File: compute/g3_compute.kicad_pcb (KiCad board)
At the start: 4 copper layers, 100 x 100 mm, 67 parts, among them J101 CONSMA001-SMD-G, J102 Temp_Connector_1x4, J103 Conn_02x03_Counter_Clockwise, J104 Conn_Power_Compute_02x05, J3 GPIO_Breakout_Conn, U101 PA1616D, U102 LoRa-E5, U201 SX1262, U202 PE4259, Y201 TBD

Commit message: changes to compute
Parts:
- moved U101 28.2 mm to (81.7, 47.2)
- moved J103 20.5 mm to (132.2, 155.2)
- moved J104 20.5 mm to (120.0, 155.2)
- moved J3 20.5 mm to (105.5, 155.1)
- moved J102 20.3 mm to (156.6, 21.8)

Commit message: fixes to power and compute
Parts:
- removed the C102 at (186.2, 69.0)
- removed the C102 at (192.2, 20.5)
- removed C201: 470nF, Capacitor_SMD:C_0402_1005Metric_Pad0.74x0.62mm_HandSolder
- removed C202: 100nF, Capacitor_SMD:C_0402_1005Metric_Pad0.74x0.62mm_HandSolder
- removed C203: 1uF, Capacitor_SMD:C_0402_1005Metric_Pad0.74x0.62mm_HandSolder
- removed C204: 47nF, Capacitor_SMD:C_0402_1005Metric_Pad0.74x0.62mm_HandSolder
- removed C205: 47pF, Capacitor_SMD:C_0402_1005Metric_Pad0.74x0.62mm_HandSolder
- removed C206, C213: 1.8pF, Capacitor_SMD:C_0402_1005Metric_Pad0.74x0.62mm_HandSolder
- removed C207, C210: 4.7pF, Capacitor_SMD:C_0402_1005Metric_Pad0.74x0.62mm_HandSolder
- removed C208: 2.4pF, Capacitor_SMD:C_0402_1005Metric_Pad0.74x0.62mm_HandSolder
- removed C209: 3pF, Capacitor_SMD:C_0402_1005Metric_Pad0.74x0.62mm_HandSolder
- removed C211: 5.6pF, Capacitor_SMD:C_0402_1005Metric_Pad0.74x0.62mm_HandSolder
- removed C212, C215: 39pF, Capacitor_SMD:C_0402_1005Metric_Pad0.74x0.62mm_HandSolder
- removed C214: 1nF, Capacitor_SMD:C_0402_1005Metric_Pad0.74x0.62mm_HandSolder
- removed C216, C217: 3.3pF, Capacitor_SMD:C_0402_1005Metric_Pad0.74x0.62mm_HandSolder
- removed J103: Conn_02x03_Counter_Clockwise, Connector_Samtec_HLE_SMD:Samtec_HLE-103-02-xxx-DV_2x03_P2.54mm_Horizontal
- removed J104: Conn_Power_Compute_02x05, Connector_Samtec_HLE_SMD:Samtec_HLE-105-02-xxx-DV_2x05_P2.54mm_Horizontal
- removed J3: GPIO_Breakout_Conn, Connector_Samtec_HLE_SMD:Samtec_HLE-105-02-xxx-DV_2x05_P2.54mm_Horizontal
- removed L201: 15uH, Inductor_SMD:L_0805_2012Metric_Pad1.05x1.20mm_HandSolder
- removed L202: 0H, Inductor_SMD:L_0402_1005Metric_Pad0.77x0.64mm_HandSolder
- removed L203: 15nH, Inductor_SMD:L_0402_1005Metric_Pad0.77x0.64mm_HandSolder
- removed L204: 47nH, Inductor_SMD:L_0402_1005Metric_Pad0.77x0.64mm_HandSolder
- removed L205: 2.5nH, Inductor_SMD:L_0402_1005Metric_Pad0.77x0.64mm_HandSolder
- removed L206: 4.7nH, Inductor_SMD:L_0402_1005Metric_Pad0.77x0.64mm_HandSolder
- removed L207: 9.1nH, Inductor_SMD:L_0402_1005Metric_Pad0.77x0.64mm_HandSolder
- removed R201: 100, Resistor_SMD:R_0402_1005Metric_Pad0.72x0.64mm_HandSolder
- removed TP110: TestPoint, Capacitor_SMD:C_0805_2012Metric_Pad1.18x1.45mm_HandSolder
- removed U201: SX1262, Package_DFN_QFN:QFN-24-1EP_4x4mm_P0.5mm_EP2.7x2.7mm
- removed U202: PE4259, Package_TO_SOT_SMD:SOT-363_SC-70-6
- removed Y201: TBD, Crystal:Crystal_SMD_2016-4Pin_2.0x1.6mm
- added C102: 4.7uF, Capacitor_SMD:C_0402_1005Metric_Pad0.74x0.62mm_HandSolder, F.Cu at (151.4, 51.7)
- added J1: Conn_01x10_Female, Connector_Molex:Molex_CLIK-Mate_502386-1070_1x10-1MP_P1.25mm_Horizontal, F.Cu at (138.7, 98.5)
- added J2: Conn_01x10_Female, Connector_Molex:Molex_CLIK-Mate_502386-1070_1x10-1MP_P1.25mm_Horizontal, F.Cu at (138.8, 119.9)
- added TP1: TestPoint, Capacitor_SMD:C_0805_2012Metric_Pad1.18x1.45mm_HandSolder, F.Cu at (160.5, 148.1)
- added TP2: TestPoint, Capacitor_SMD:C_0805_2012Metric_Pad1.18x1.45mm_HandSolder, F.Cu at (150.9, 148.1)
- added TP3: TestPoint, Capacitor_SMD:C_0805_2012Metric_Pad1.18x1.45mm_HandSolder, F.Cu at (155.7, 145.1)
- moved U101 115.6 mm to (190.7, 85.9), turned to 90 degrees
- moved J101 98.0 mm to (192.3, 143.7), turned to 270 degrees
- moved J102 94.8 mm to (187.1, 111.6), turned to 90 degrees
- moved R301 94.5 mm to (161.5, 47.7)
- moved C104 93.4 mm to (186.6, 143.9), turned to 270 degrees
- moved C103 89.3 mm to (184.7, 140.6), turned to 270 degrees
- moved L101 88.3 mm to (186.6, 140.6), turned to 270 degrees
- moved TP115 87.6 mm to (170.1, 148.1), turned to 0 degrees
- moved TP103 84.7 mm to (160.5, 145.1), turned to 0 degrees
- moved TP106 82.6 mm to (165.3, 145.1), turned to 0 degrees
- moved TP112 82.6 mm to (170.1, 145.1), turned to 0 degrees
- moved TP114 82.4 mm to (165.3, 151.1), turned to 0 degrees
- moved TP105 80.5 mm to (155.7, 151.1), turned to 0 degrees
- moved TP111 79.8 mm to (165.3, 148.1), turned to 0 degrees
- moved R101 79.5 mm to (144.9, 47.7)
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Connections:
- net /GPS_VCC renamed /GPS_Switch/VOUT
- net 3V3 renamed +3V3
- net 5V renamed +5V
- A101 pad 11: /PI_GPIO17 -> /PS_VSolSense
- A101 pad 12: /PI_GPIO18 -> /~PS_CC_QON
- A101 pad 16: /PI_GPIO23 -> /~PS_CC_INT
- A101 pad 18: /PI_GPIO24 -> /~PC_CC_CE
- A101 pad 22: /PI_GPIO25 -> /PS_VR_PS
- A101 pad 32: /PI_INT -> /CPPC_INT
- A101 pad 7: /PI_GPIO4 -> /PS_VBatSense
- J102 pad 4: /PI_SDL -> /PI_SCL
- R104 pad 1: /PI_SDL -> /PI_SCL
- TP109 pad 1: /PI_SDL -> /PI_SCL
- U102 pad 16: Net-(U102-Pad16) -> GND
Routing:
- net GND: track 53.4 -> 0.00 mm, vias 15 -> 0
- net /ANT: track 21.9 -> 0.00 mm
- net Net-(C204-Pad1): track 7.09 -> 0.00 mm
- net +3V3: track 6.70 -> 0.00 mm, vias 3 -> 0
- net Net-(U201-Pad4): track 6.52 -> 0.00 mm
- net Net-(C214-Pad1): track 6.44 -> 0.00 mm
- net Net-(C207-Pad1): track 5.38 -> 0.00 mm
- net Net-(C201-Pad1): track 5.19 -> 0.00 mm
- net Net-(L202-Pad1): track 5.07 -> 0.00 mm
- net Net-(C206-Pad1): track 4.97 -> 0.00 mm
- net Net-(L203-Pad1): track 4.14 -> 0.00 mm
- net Net-(C209-Pad2): track 3.58 -> 0.00 mm
- net Net-(U201-Pad3): track 3.58 -> 0.00 mm
- net Net-(L201-Pad2): track 2.79 -> 0.00 mm
- net Net-(C213-Pad1): track 2.60 -> 0.00 mm
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- added copper zone on 3V3, net 3V3
- removed copper zone on 3V3, net +3V3
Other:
- board text removed: "LoRa-E5"
- board text removed: "SX1612"

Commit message: Started compute board layout
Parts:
- removed A101: ADA3708, Perch:ADA3708_RaspPiZero
- removed J1, J2: Conn_01x10_Female, Connector_Molex:Molex_CLIK-Mate_502386-1070_1x10-1MP_P1.25mm_Horizontal
- removed L101: 0, Inductor_SMD:L_0402_1005Metric_Pad0.77x0.64mm_HandSolder
- removed R301: TBD, Resistor_SMD:R_0402_1005Metric_Pad0.72x0.64mm_HandSolder
- removed TP1, TP2, TP3: TestPoint, Capacitor_SMD:C_0805_2012Metric_Pad1.18x1.45mm_HandSolder
- added C106: 1uF, Capacitor_SMD:C_0402_1005Metric_Pad0.74x0.62mm_HandSolder, F.Cu at (127.4, 84.0)
- added C107: DNL, Capacitor_SMD:C_0402_1005Metric_Pad0.74x0.62mm_HandSolder, F.Cu at (90.0, 104.0)
- added C108: DNL, Capacitor_SMD:C_0402_1005Metric_Pad0.74x0.62mm_HandSolder, F.Cu at (90.0, 92.0)
- added C201: 470nF, Capacitor_SMD:C_0402_1005Metric_Pad0.74x0.62mm_HandSolder, F.Cu at (6.01, 148.2)
- added C202: 100nF, Capacitor_SMD:C_0402_1005Metric_Pad0.74x0.62mm_HandSolder, F.Cu at (12.3, 144.2)
- added C203: 1uF, Capacitor_SMD:C_0402_1005Metric_Pad0.74x0.62mm_HandSolder, F.Cu at (9.09, 144.2)
- added C204: 47nF, Capacitor_SMD:C_0402_1005Metric_Pad0.74x0.62mm_HandSolder, F.Cu at (9.22, 150.1)
- added C205: 47pF, Capacitor_SMD:C_0402_1005Metric_Pad0.74x0.62mm_HandSolder, F.Cu at (9.22, 148.2)
- added C206: 1.8pF, Capacitor_SMD:C_0402_1005Metric_Pad0.74x0.62mm_HandSolder, F.Cu at (6.01, 150.1)
- added C207: 4.7pF, Capacitor_SMD:C_0402_1005Metric_Pad0.74x0.62mm_HandSolder, F.Cu at (11.5, 146.2)
- added C208: 2.4pF, Capacitor_SMD:C_0402_1005Metric_Pad0.74x0.62mm_HandSolder, F.Cu at (-0.41, 150.2)
- added C209: 3pF, Capacitor_SMD:C_0402_1005Metric_Pad0.74x0.62mm_HandSolder, F.Cu at (5.88, 142.3)
- added C210: 4.7pF, Capacitor_SMD:C_0402_1005Metric_Pad0.74x0.62mm_HandSolder, F.Cu at (5.08, 146.2)
- added C211: 5.6pF, Capacitor_SMD:C_0402_1005Metric_Pad0.74x0.62mm_HandSolder, F.Cu at (2.80, 150.1)
- added C212: 39pF, Capacitor_SMD:C_0402_1005Metric_Pad0.74x0.62mm_HandSolder, F.Cu at (9.09, 142.3)
- added C213: 1.8pF, Capacitor_SMD:C_0402_1005Metric_Pad0.74x0.62mm_HandSolder, F.Cu at (5.88, 144.2)
- added C214: 1nF, Capacitor_SMD:C_0402_1005Metric_Pad0.74x0.62mm_HandSolder, F.Cu at (10.1, 140.3)
- added C215: 39pF, Capacitor_SMD:C_0402_1005Metric_Pad0.74x0.62mm_HandSolder, F.Cu at (1.83, 148.1)
- added C216: 3.3pF, Capacitor_SMD:C_0402_1005Metric_Pad0.74x0.62mm_HandSolder, F.Cu at (8.29, 146.2)
- added C217: 3.3pF, Capacitor_SMD:C_0402_1005Metric_Pad0.74x0.62mm_HandSolder, F.Cu at (12.3, 142.2)
- added FB101: GMLB-100505, Resistor_SMD:R_0402_1005Metric_Pad0.72x0.64mm_HandSolder, F.Cu at (82.0, 101.0)
- added H101: MountingHole_Pad, MountingHole:MountingHole_2.5mm_Pad, F.Cu at (105.0, 55.0)
- added H102: MountingHole_Pad, MountingHole:MountingHole_2.5mm_Pad, F.Cu at (195.0, 55.0)
- added H103: MountingHole_Pad, MountingHole:MountingHole_2.5mm_Pad, F.Cu at (105.0, 145.0)
- added H104: MountingHole_Pad, MountingHole:MountingHole_2.5mm_Pad, F.Cu at (195.0, 145.0)
- added IC101: CD74AC153M96, Perch:SOIC127P600X175-16N_MUX, F.Cu at (130.0, 73.0)
- added J103: Temp_Connector_1x4, Perch:1702474_Temp_Sensor_Connector, F.Cu at (187.0, 61.0)
- added J104: 53398-0671, Perch:533980671_Molex, F.Cu at (144.0, 54.0)
- added J105: Conn_01x10_Male, Connector_PinHeader_2.54mm:PinHeader_1x10_P2.54mm_Vertical, F.Cu at (105.0, 111.0)
- added J106: Pi_Connector, Module:Raspberry_Pi_Zero_Socketed_THT_FaceDown_MountingHoles, F.Cu at (151.2, 75.8)
- added J107: Conn_01x06_Male, Connector_PinHeader_2.54mm:PinHeader_1x06_P2.54mm_Vertical, F.Cu at (105.0, 65.0)
- added J108: CONSMA001-SMD-G, digikey-footprints:RF_SMA_Receptical_Vertical_CONSMA001-SMD-G, F.Cu at (116.0, 144.0)
- added J109: CONSMA001-SMD-G, digikey-footprints:RF_SMA_Receptical_Vertical_CONSMA001-SMD-G, F.Cu at (142.0, 144.0)
- added J110: CONSMA001-SMD-G, digikey-footprints:RF_SMA_Receptical_Vertical_CONSMA001-SMD-G, F.Cu at (129.0, 144.0)
- added JP101: SolderJumper_2_Bridged, Jumper:SolderJumper-2_P1.3mm_Bridged_RoundedPad1.0x1.5mm, F.Cu at (80.3, 111.0)
- added JP102: SolderJumper_2_Bridged, Jumper:SolderJumper-2_P1.3mm_Bridged_RoundedPad1.0x1.5mm, F.Cu at (73.3, 115.0)
- added JP103: SolderJumper_2_Bridged, Jumper:SolderJumper-2_P1.3mm_Bridged_RoundedPad1.0x1.5mm, F.Cu at (66.0, 128.0)
- added JP104: SolderJumper_2_Bridged, Jumper:SolderJumper-2_P1.3mm_Bridged_RoundedPad1.0x1.5mm, F.Cu at (62.0, 134.0)
- added L201: 15uH, Inductor_SMD:L_0805_2012Metric_Pad1.05x1.20mm_HandSolder, F.Cu at (-6.07, 146.9)
- added L202: 0H, Inductor_SMD:L_0402_1005Metric_Pad0.77x0.64mm_HandSolder, F.Cu at (3.65, 140.3)
- added L203: 15nH, Inductor_SMD:L_0402_1005Metric_Pad0.77x0.64mm_HandSolder, F.Cu at (-0.60, 144.1)
- added L204: 47nH, Inductor_SMD:L_0402_1005Metric_Pad0.77x0.64mm_HandSolder, F.Cu at (-3.64, 150.2)
- added L205: 2.5nH, Inductor_SMD:L_0402_1005Metric_Pad0.77x0.64mm_HandSolder, F.Cu at (6.90, 140.3)
- added L206: 4.7nH, Inductor_SMD:L_0402_1005Metric_Pad0.77x0.64mm_HandSolder, F.Cu at (1.85, 146.1)
- added L207: 9.1nH, Inductor_SMD:L_0402_1005Metric_Pad0.77x0.64mm_HandSolder, F.Cu at (2.65, 144.1)
- added Q101: PBSS4140DPN, Perch:PBSS4140DPN, F.Cu at (129.6, 114.0)
- added R109: 10k, Resistor_SMD:R_0402_1005Metric_Pad0.72x0.64mm_HandSolder, F.Cu at (73.5, 138.5)
- added R201: 100, Resistor_SMD:R_0402_1005Metric_Pad0.72x0.64mm_HandSolder, F.Cu at (-6.89, 149.3)
- added S101: 452403012014, Perch:452403012014_Switch, F.Cu at (116.4, 73.5)
- added TP110: TestPoint, Capacitor_SMD:C_0805_2012Metric_Pad1.18x1.45mm_HandSolder, F.Cu at (49.6, 112.0)
- added TP116: TestPoint, Capacitor_SMD:C_0805_2012Metric_Pad1.18x1.45mm_HandSolder, F.Cu at (39.4, 117.5)
- added TP117: TestPoint, Capacitor_SMD:C_0805_2012Metric_Pad1.18x1.45mm_HandSolder, F.Cu at (27.5, 128.6)
- added TP118: TestPoint, Capacitor_SMD:C_0805_2012Metric_Pad1.18x1.45mm_HandSolder, F.Cu at (32.3, 125.6)
- added TP119: TestPoint, Capacitor_SMD:C_0805_2012Metric_Pad1.18x1.45mm_HandSolder, F.Cu at (44.8, 110.3)
- added TP120: TestPoint, Capacitor_SMD:C_0805_2012Metric_Pad1.18x1.45mm_HandSolder, F.Cu at (43.1, 114.5)
- added TP121: TestPoint, Capacitor_SMD:C_0805_2012Metric_Pad1.18x1.45mm_HandSolder, F.Cu at (71.3, 72.3)
- added TP122: TestPoint, Capacitor_SMD:C_0805_2012Metric_Pad1.18x1.45mm_HandSolder, F.Cu at (81.2, 76.3)
- added TP123: TestPoint, Capacitor_SMD:C_0805_2012Metric_Pad1.18x1.45mm_HandSolder, F.Cu at (86.8, 70.0)
- added TP124: TestPoint, Capacitor_SMD:C_0805_2012Metric_Pad1.18x1.45mm_HandSolder, F.Cu at (91.6, 67.0)
- added TP125: TestPoint, Capacitor_SMD:C_0805_2012Metric_Pad1.18x1.45mm_HandSolder, F.Cu at (49.6, 109.0)
- added TP126: TestPoint, Capacitor_SMD:C_0805_2012Metric_Pad1.18x1.45mm_HandSolder, F.Cu at (86.8, 67.0)
- added TP127: TestPoint, Capacitor_SMD:C_0805_2012Metric_Pad1.18x1.45mm_HandSolder, F.Cu at (75.3, 75.4)
- added TP128: TestPoint, Capacitor_SMD:C_0805_2012Metric_Pad1.18x1.45mm_HandSolder, F.Cu at (38.3, 114.5)
- added TP129: TestPoint, Capacitor_SMD:C_0805_2012Metric_Pad1.18x1.45mm_HandSolder, F.Cu at (44.8, 107.3)
- added TP130: TestPoint, Capacitor_SMD:C_0805_2012Metric_Pad1.18x1.45mm_HandSolder, F.Cu at (43.4, 104.3)
- added TP131: TestPoint, Capacitor_SMD:C_0805_2012Metric_Pad1.18x1.45mm_HandSolder, F.Cu at (86.8, 76.1)
- added TP132: TestPoint, Capacitor_SMD:C_0805_2012Metric_Pad1.18x1.45mm_HandSolder, F.Cu at (61.2, 102.7)
- added TP133: TestPoint, Capacitor_SMD:C_0805_2012Metric_Pad1.18x1.45mm_HandSolder, F.Cu at (96.4, 67.0)
- added TP134: TestPoint, Capacitor_SMD:C_0805_2012Metric_Pad1.18x1.45mm_HandSolder, F.Cu at (44.2, 117.5)
- added TP135: TestPoint, Capacitor_SMD:C_0805_2012Metric_Pad1.18x1.45mm_HandSolder, F.Cu at (68.7, 81.8)
- added TP136: TestPoint, Capacitor_SMD:C_0805_2012Metric_Pad1.18x1.45mm_HandSolder, F.Cu at (39.4, 123.5)
- added TP137: TestPoint, Capacitor_SMD:C_0805_2012Metric_Pad1.18x1.45mm_HandSolder, F.Cu at (27.5, 134.6)
- added U201: SX1262, Package_DFN_QFN:QFN-24-1EP_4x4mm_P0.5mm_EP2.7x2.7mm, F.Cu at (-5.37, 142.4)
- added U202: PE4259, Package_TO_SOT_SMD:SOT-363_SC-70-6, F.Cu at (-0.10, 141.2)
- added Y201: TBD, Crystal:Crystal_SMD_2016-4Pin_2.0x1.6mm, F.Cu at (-1.70, 147.4)
- C101, C105: value 1uF -> 0.1uF
- C102: value 4.7uF -> 1uF
- C103: value DNL -> 0.1uF
- C104: value DNL -> 4.7uF
- J101: value CONSMA001-SMD-G -> Conn_01x09_Male; footprint digikey-footprints:RF_SMA_Receptical_Vertical_CONSMA001-SMD-G -> Connector_PinHeader_2.54mm:PinHeader_1x09_P2.54mm_Vertical
- J102: value Temp_Connector_1x4 -> 53398-0871; footprint Perch:1702474_Temp_Sensor_Connector -> Perch:53398-0871_Molex
- R101: value 470 -> 4.7k
- R102: value 470 -> DNL
- R103: value TBD -> DNL
- R104: value TBD -> 4.7k
- R105: value 0 -> 10k
- R106: value 0 -> 1.62k; footprint Resistor_SMD:R_0402_1005Metric_Pad0.72x0.64mm_HandSolder -> Resistor_SMD:R_0603_1608Metric_Pad0.98x0.95mm_HandSolder
- R107: value 22 -> 0
- R108: value 22 -> 10k
- U101: value PA1616D -> LoRa-E5; footprint Perch:PA1616D_GPS -> Perch:LoRa-E5
- U102: value LoRa-E5 -> PA1616D; footprint Perch:LoRa-E5 -> Perch:PA1616D_GPS
- moved TP114 140.2 mm to (27.5, 125.6)
- moved TP115 139.2 mm to (32.3, 128.6)
- moved TP101 124.9 mm to (27.5, 131.6)
- moved TP103 123.6 mm to (39.4, 120.5)
- moved R106 121.6 mm to (69.9, 138.0)
- moved TP112 121.2 mm to (54.5, 109.0)
- moved R108 116.1 mm to (76.7, 138.5)
- moved TP102 115.4 mm to (71.3, 69.3)
- moved TP108 114.0 mm to (70.5, 78.4)
- moved TP113 112.5 mm to (68.9, 88.8)
- moved R105 112.0 mm to (80.0, 138.5)
- moved TP105 107.5 mm to (61.2, 99.7)
- moved TP109 107.4 mm to (86.8, 73.0)
- moved TP111 107.4 mm to (91.6, 70.0)
- moved TP106 106.8 mm to (81.2, 79.3)
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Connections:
- C101 pad 2: /GPS_Switch/VOUT -> V_GPS
- C102 pad 1: +3V3 -> GND
- C102 pad 2: GND -> V_GPS
- C103 pad 1: /E5_RFIO -> GND
- C103 pad 2: GND -> +3V3
- C104 pad 1: /ANT -> +3V3
- C105 pad 2: +3V3 -> +5V
- J101 pad 1: GND -> /~SX_CS
- J101 pad 2: /ANT -> /SX_SCK
- J102 pad 1: +3V3 -> +5V
- J102 pad 3: /PI_SDA -> /PS_BOOST_PS
- J102 pad 4: /PI_SCL -> /~PS_CC_INT
- J102 pad 5: (no net) -> /~PS_CC_CE
- J102 pad 6: (no net) -> /~PS_CC_QON
- R101 pad 1: /GPS_RX0 -> /PI_SDA
- R101 pad 2: /PI_TX0 -> +3V3
- R102 pad 1: /GPS_TX0 -> /PI_SDA
- R102 pad 2: /PI_RX0 -> +3V3
- R103 pad 1: /PI_SDA -> /PI_SCL
- R105 pad 1: /CPPC_RX0 -> /~GPS_RESET
- R105 pad 2: /PI_TX1 -> +3V3
- R106 pad 1: /CPPC_TX0 -> Net-(Q101-Pad2)
- R106 pad 2: /PI_RX1 -> /GPS_SW_EN
- R107 pad 1: /E5_RX -> /E5_RFIO
- R107 pad 2: /PI_TX2 -> /ANT
- R108 pad 1: /E5_TX -> GND
- R108 pad 2: /PI_RX2 -> /MUX_SELA
- TP101 pad 1: +5V -> /E5_TX
- TP102 pad 1: /PI_SDI -> /E5_RX
- TP103 pad 1: GND -> /~E5_RESET
- TP104 pad 1: /PI_SDO -> /GPS_TX
- TP105 pad 1: +3V3 -> /GPS_RX
- TP106 pad 1: /PI_SCLK -> /~GPS_RESET
- TP107 pad 1: /PI_SDA -> /GPS_SW_EN
- TP108 pad 1: /~PI_CE0 -> /GPS_3DFIX
- TP109 pad 1: /PI_SCL -> /CPPC_TX
- TP111 pad 1: /~E5_RESET -> /PI_SDA
- TP112 pad 1: /PI_TX0 -> /PI_SCL
- TP113 pad 1: /PI_RX0 -> /Temp_SDA
- TP114 pad 1: /PI_TX2 -> /Temp_SCL
- TP115 pad 1: /PI_RX2 -> /PS_CC_SDA
- U101 pad 1: /GPS_Switch/VOUT -> +3V3
- U101 pad 10: /GPS_RX0 -> /E5_TX
- U101 pad 12: GND -> Net-(U101-Pad12)
- U101 pad 14: Net-(U101-Pad14) -> GND
- U101 pad 15: Net-(U101-Pad15) -> /E5_RFIO
- U101 pad 16: Net-(U101-Pad16) -> GND
- U101 pad 17: Net-(U101-Pad17) -> /~E5_RESET
- U101 pad 19: GND -> Net-(U101-Pad19)
- U101 pad 2: /~GPS_RESET -> GND
- U101 pad 3: GND -> Net-(U101-Pad3)
- U101 pad 8: GND -> Net-(U101-Pad8)
- U101 pad 9: /GPS_TX0 -> /E5_RX
- U102 pad 1: +3V3 -> V_GPS
- U102 pad 10: /E5_TX -> /GPS_RX
- U102 pad 12: Net-(U102-Pad12) -> GND
- U102 pad 14: GND -> Net-(U102-Pad14)
- U102 pad 15: /E5_RFIO -> Net-(U102-Pad15)
- U102 pad 16: GND -> Net-(U102-Pad16)
- U102 pad 17: /~E5_RESET -> Net-(U102-Pad17)
- U102 pad 19: Net-(U102-Pad19) -> GND
- U102 pad 2: GND -> /~GPS_RESET
- U102 pad 3: Net-(U102-Pad3) -> GND
- U102 pad 5: Net-(U102-Pad5) -> /GPS_3DFIX
- U102 pad 8: Net-(U102-Pad8) -> GND
- U102 pad 9: /E5_RX -> /GPS_TX
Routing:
- removed copper zone on 3V3, net 3V3

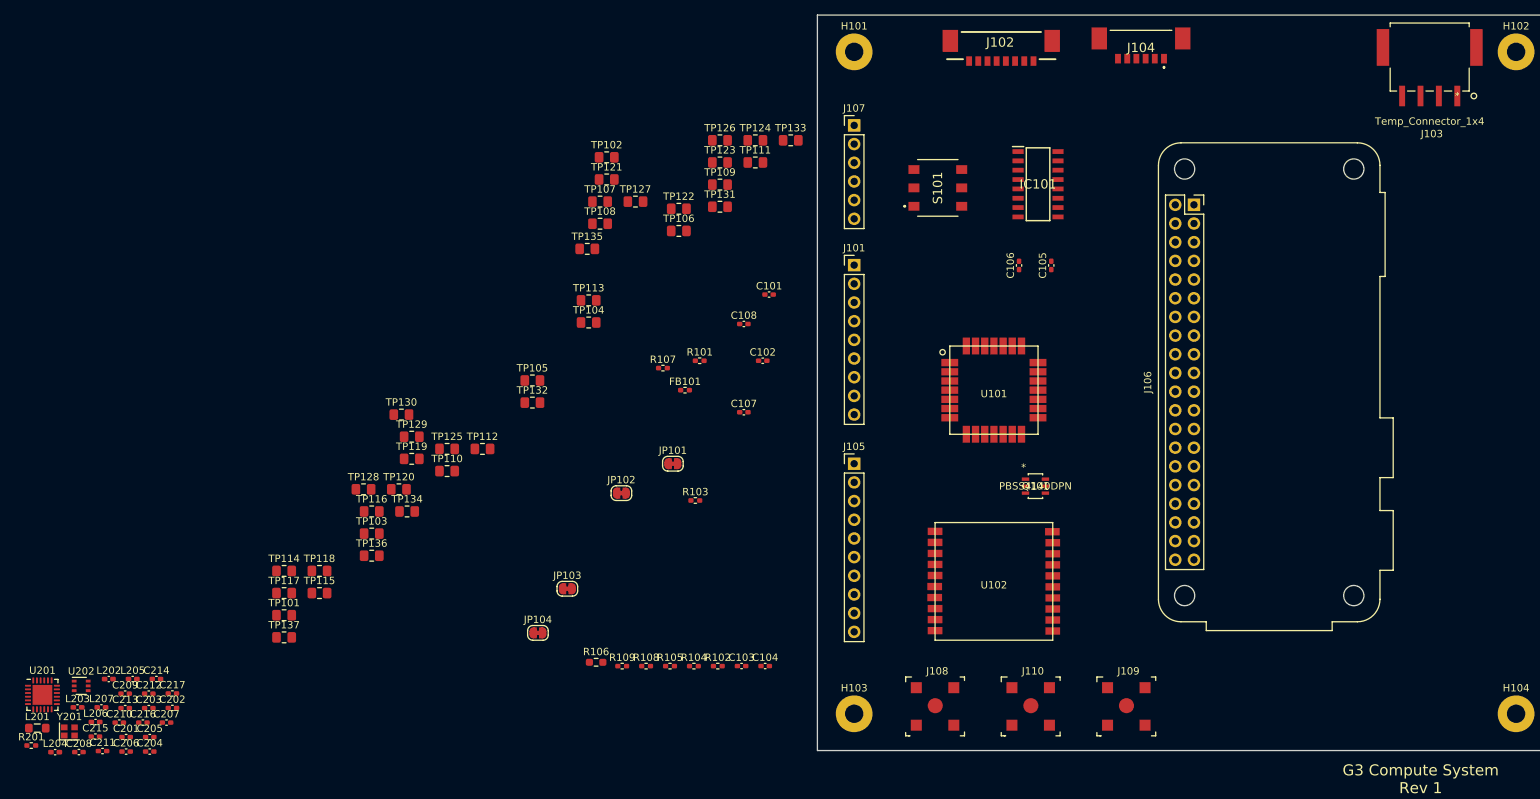
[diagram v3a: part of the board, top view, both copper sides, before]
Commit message: Moved all parts around for PCB layout except second LoRa module
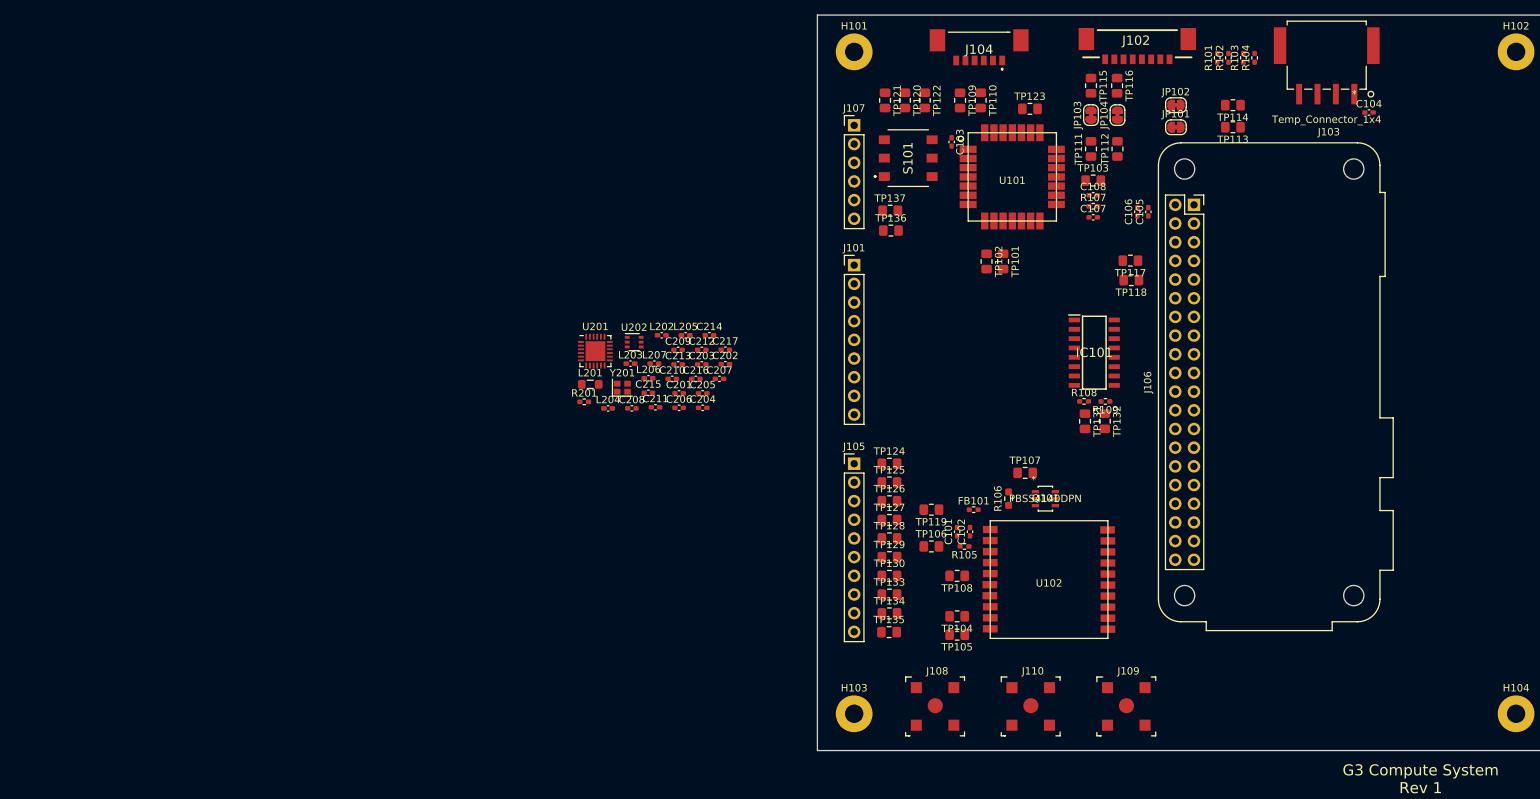
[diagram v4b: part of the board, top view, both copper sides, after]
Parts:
- moved TP114 143.7 mm to (156.5, 62.2), turned to 180 degrees
- moved TP115 125.6 mm to (137.2, 59.6), turned to 270 degrees
- moved TP117 123.6 mm to (142.6, 83.4), turned to 180 degrees
- moved TP118 117.3 mm to (142.7, 86.0), turned to 180 degrees
- moved TP116 116.7 mm to (140.8, 59.6), turned to 270 degrees
- moved R104 112.5 mm to (159.4, 55.8), turned to 90 degrees
- moved C104 111.4 mm to (175.0, 63.2)
- moved TP103 109.2 mm to (137.5, 72.5)
- moved TP101 109.0 mm to (125.2, 83.5), turned to 270 degrees
- moved R102 108.0 mm to (155.9, 55.8), turned to 90 degrees
- moved JP104 105.7 mm to (140.8, 63.6), turned to 90 degrees
- moved TP137 100.8 mm to (109.9, 76.6)
- moved JP103 96.0 mm to (137.2, 63.6), turned to 90 degrees
- moved R103 95.8 mm to (157.9, 55.8), turned to 90 degrees
- moved TP112 95.5 mm to (140.8, 68.2), turned to 90 degrees
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
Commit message: Changed pinout to GPIO Connector to make routing easier
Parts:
- TP101, TP102, TP103, TP104, TP105, TP106, TP107, TP108, TP109, TP110, TP111, TP112, TP113, TP114, TP115, TP116, TP117, TP118, TP119, TP120, TP121, TP122, TP123, TP124, TP125, TP126, TP127, TP128, TP129, TP130, TP131, TP132, TP133, TP134, TP135, TP136, TP137: footprint Capacitor_SMD:C_0805_2012Metric_Pad1.18x1.45mm_HandSolder -> Perch:HARWIN_S2751-46R
- moved C201 144.9 mm to (224.8, 121.3)
- moved C202 144.9 mm to (231.0, 117.4)
- moved C203 144.9 mm to (227.8, 117.4)
- moved C204 144.9 mm to (228.0, 123.3)
- moved C205 144.9 mm to (228.0, 121.3)
- moved C206 144.9 mm to (224.8, 123.3)
- moved C207 144.9 mm to (230.2, 119.4)
- moved C208 144.9 mm to (218.3, 123.4)
- moved C209 144.9 mm to (224.6, 115.4)
- moved C210 144.9 mm to (223.8, 119.4)
- moved C211 144.9 mm to (221.5, 123.2)
- moved C212 144.9 mm to (227.8, 115.4)
- moved C213 144.9 mm to (224.6, 117.4)
- moved C214 144.9 mm to (228.9, 113.4)
- moved C215 144.9 mm to (220.6, 121.3)
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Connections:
- J105 pad 1: /PI_GPIO8 -> /PI_GPIO17
- J105 pad 2: /PI_GPIO9 -> /PI_GPIO22
- J105 pad 4: /PI_GPIO11 -> /PI_GPIO25
- J105 pad 5: /PI_GPIO13 -> /PI_GPIO9
- J105 pad 6: /PI_GPIO17 -> /PI_GPIO8
- J105 pad 7: /PI_GPIO19 -> /PI_GPIO11
- J105 pad 8: /PI_GPIO22 -> /PI_GPIO13
- J105 pad 9: /PI_GPIO25 -> /PI_GPIO19
